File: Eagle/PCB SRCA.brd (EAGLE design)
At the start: 160 x 100 mm, 75 parts, among them IC1 DSPIC30F4011-30I_P, IC2 LM324LVIDR, IC3 LMT86QDCKRQ1, IC5 FT232RL-REEL, J1 TBL002A-350-03GR-2OR, J2 TBL002A-350-03GR-2OR, J3 TBL002A-350-03GR-2OR, J4 44914-0801, J6 TBL002A-350-03GR-2OR, J7 44914-0401, Q1 TIP41C, T1 2N3904, T12 2N3904, T13 2N3904, T2 2N3904, T3 2N3904, T4 2N3904, T5 2N3904, T6 2N3904, T7 2N3904

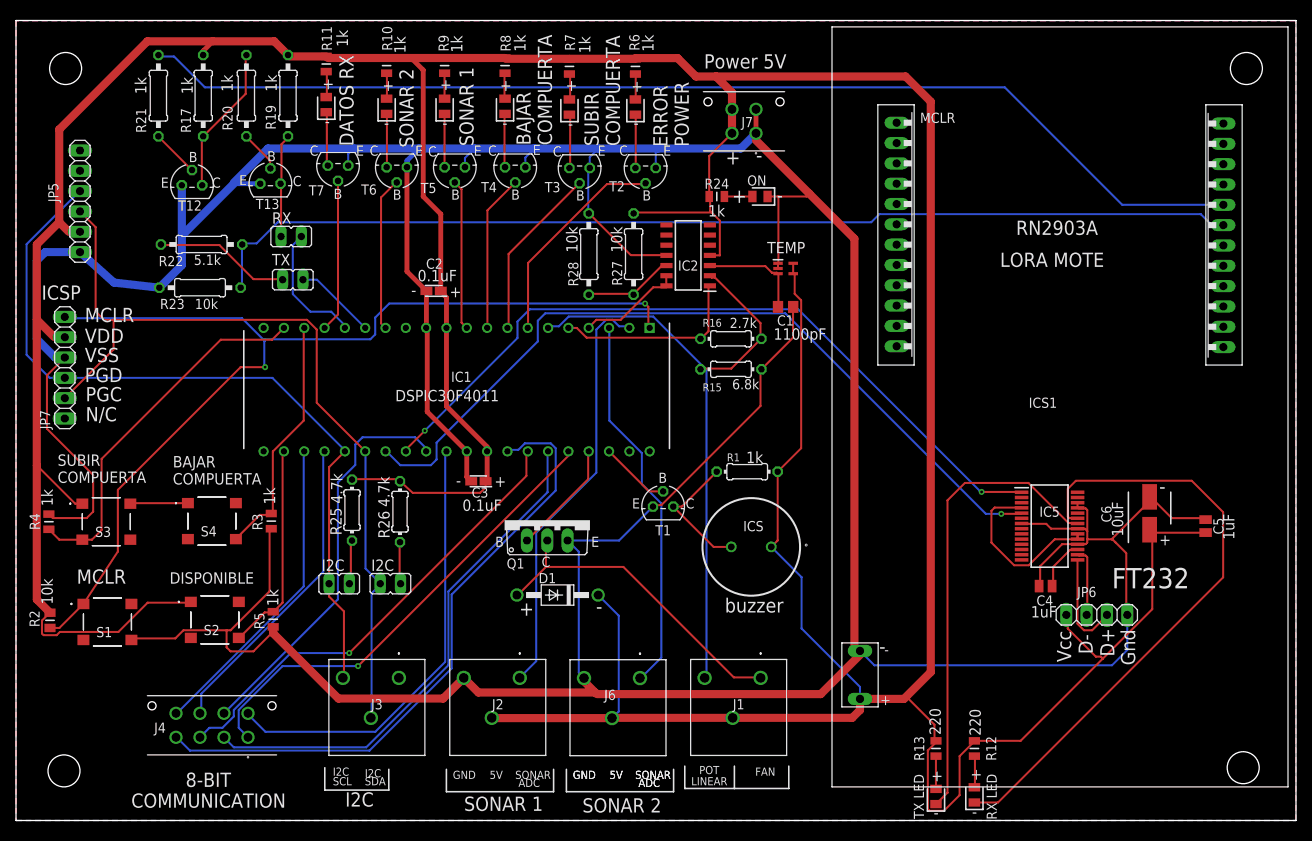
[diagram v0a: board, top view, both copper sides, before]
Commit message: 24-08-2021
correccion de errores en pistas
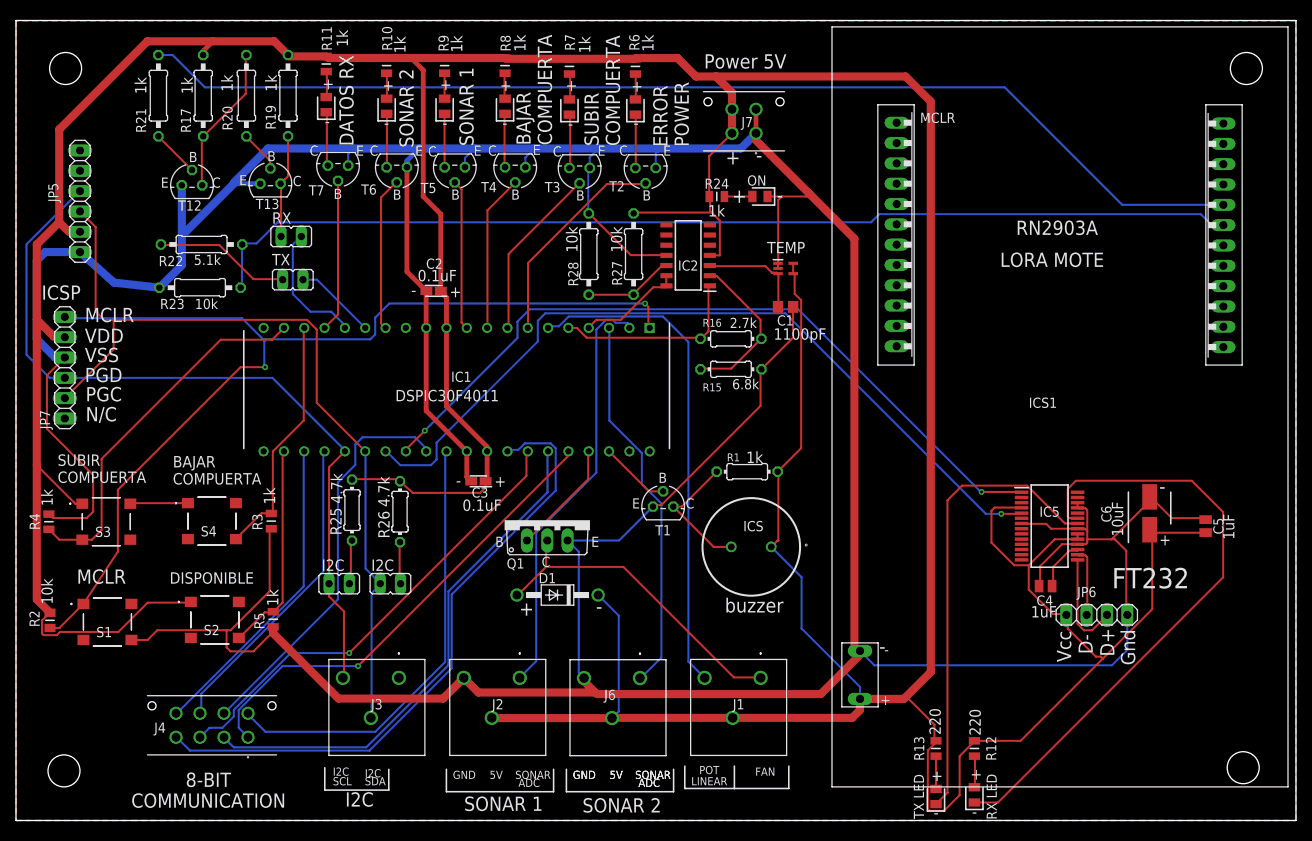
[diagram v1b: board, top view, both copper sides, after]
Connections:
- removed net N$14: IC5.19, IC5.20, IC5.4
- net V+: now also IC5.19, IC5.20, IC5.4
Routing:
- net V+: track 622.5 -> 652.4 mm
- net N$14: track 22.2 -> 0.00 mm
- net GND: track 597.9 -> 596.3 mm
- net GATE_DOWN: track 46.7 -> 46.1 mm
- net POT_LINEAR: track 61.8 -> 62.3 mm

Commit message: 26-08-2021
Actulizacion de la pcb correccion de pistas separacion entre ellas
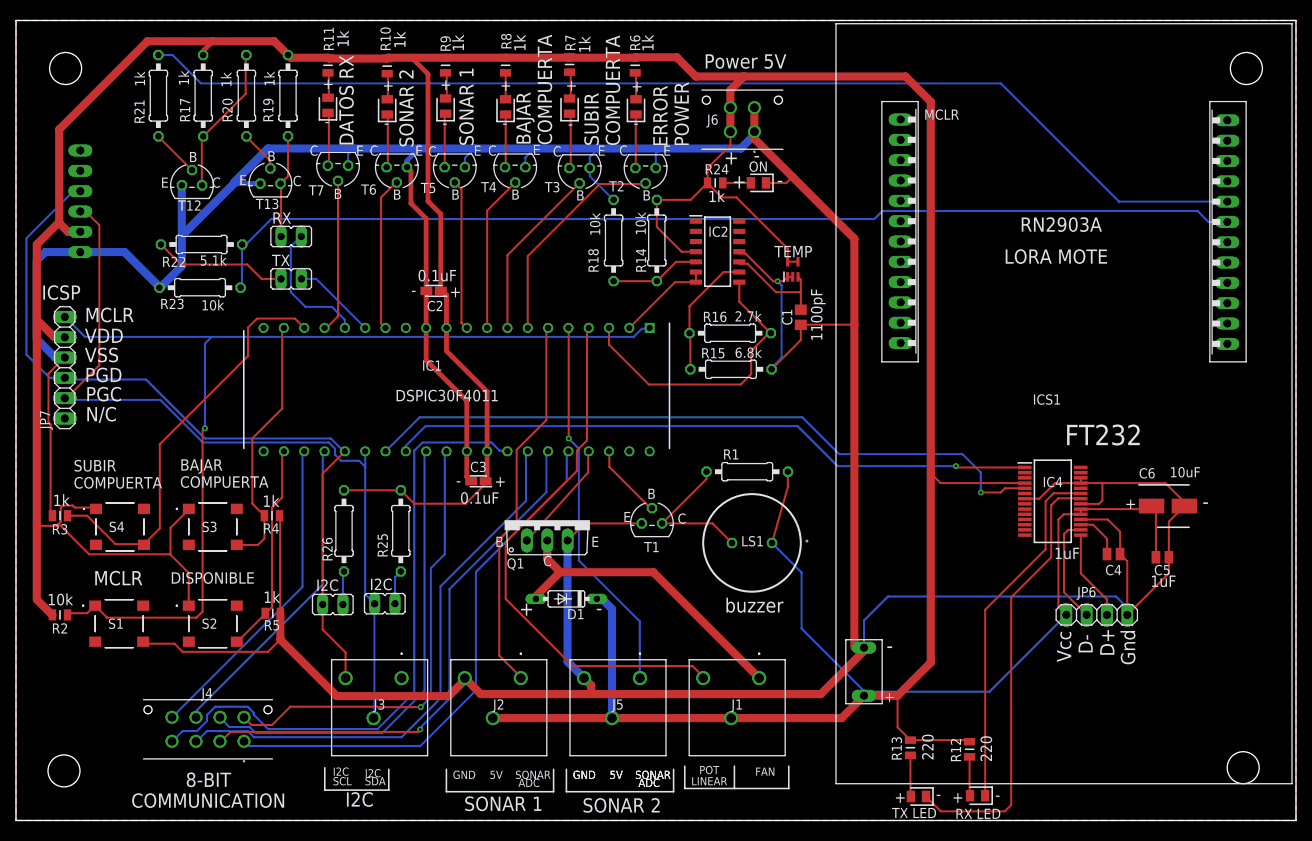
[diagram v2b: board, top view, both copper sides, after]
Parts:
- removed IC5: FT232RL-REEL, FT232RL-REEL:SOP65P778X200-28N
- removed ICS: PS1240P02BT, PS1240P02BT:PS1240P02BT
- removed J7: 44914-0401, 44914-0401:44914-0401
- removed ON: 599-0181-007F, 599-0181-007F:LEDC2012X70N
- removed R27, R28: (no value), rcl:0207/10
- added IC4: FT232RL-REEL, FT232RL-REEL:SOP65P778X200-28N
- added J5: TBL002A-350-03GR-2OR, TBL002A-350-03GR-2OR:TBL002A35003GR2OR
- added LED9: 599-0181-007F, 599-0181-007F:LEDC2012X70N
- added LS1: PS1240P02BT, PS1240P02BT:PS1240P02BT
- added R14, R18: 10k, rcl:0207/10
- D1: value 1N4004 -> 1N4148DO35-7; device diode:DO41-10 -> diode:DO35-7
- J6: value TBL002A-350-03GR-2OR -> 44914-0401; device TBL002A-350-03GR-2OR:TBL002A35003GR2OR -> 44914-0401:44914-0401
- R1: value (none) -> 1k; device rcl:0204/7 -> rcl:0207/10
- R15: value (none) -> 6.8k; device rcl:0204/7 -> rcl:0207/10
- R16: value (none) -> 2.7k; device rcl:0204/7 -> rcl:0207/10
- R17, R19, R20, R21: value (none) -> 1k
- R2: value ERA-6VEB1002V -> RC0805FR-071KL; device ERA-6VEB1002V:RESC2012X65N -> RC0805FR-071KL:RESC2012X60N
- R22: value (none) -> 5.1k
- R23: value (none) -> 10k
- R25, R26: value (none) -> 4.7k; device rcl:0204/7 -> rcl:0207/10
- moved J6 69.8 mm to (92.3, 86.1), turned to 0 degrees
- moved R4 27.9 mm to (32.0, 38.1), turned to 180 degrees
- moved R3 26.4 mm to (5.50, 38.1), turned to 0 degrees
- moved S3 13.3 mm to (24.6, 36.7)
- moved S4 11.5 mm to (13.0, 36.7)
- moved C4 9.39 mm to (137.2, 33.3), turned to 180 degrees
- moved R26 7.40 mm to (41.0, 36.2)
- moved C5 6.66 mm to (143.3, 32.9), turned to 180 degrees
- moved R25 6.63 mm to (48.1, 36.2)
- moved IC2 3.71 mm to (87.7, 71.1), turned to 0 degrees
- moved R13 3.20 mm to (111.8, 9.10)
- moved JP4 2.72 mm to (39.6, 27.0)
- moved JP3 2.60 mm to (46.1, 27.1)
- moved T1 2.52 mm to (79.5, 37.1)
- moved C6 2.47 mm to (144.0, 39.3), turned to 0 degrees
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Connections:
- removed net LMT86: C1.1, IC2.3, IC3.3
- removed net N$15 (its old number): IC5.23, LED7.1
- removed net RESISTENCIA: IC2.2, R15.2, R16.2
- removed net TEMP1: JP4.1, R25.1
- removed net TEMP2: JP3.2, R26.1
- removed net TEMP3: ICS.2, R1.1, T1.1
- new net N$19: JP3.2, R25.1
- new net N$25: LS1.2, R1.1, T1.1
- new net N$3: IC4.23, LED7.1
- new net N$31: JP4.1, R26.1
- new net N$32: IC2.5, R14.1, R18.2
- net GATE_DOWN: now also S3.D1; no longer S3.C1
- net GND: now also C5.1, IC4.18, IC4.21, IC4.25, IC4.26, IC4.7, J5.A2, J6.1, J6.3, LED9.1, R18.1; no longer C5.2, IC5.18, IC5.21, IC5.25, IC5.26, IC5.7, J6.A2, J7.1, J7.3, ON.1, R28.1
- net N$1: now also IC2.9, R15.2, R16.2; no longer S3.B1, S4.A1
- net N$18: now also IC4.22; no longer IC5.22
- net N$20: now also IC4.17; no longer IC5.17
- net N$21: now also IC4.16; no longer IC5.16
- net N$22: now also IC4.15; no longer IC5.15
- net N$27: now also C1.1, IC2.10, IC3.3; no longer IC2.12, R27.1, R28.2
- net N$28: now also LED9.2; no longer ON.2
- net POT_LINEAR: now also IC1.4; no longer IC1.6
- net POWER: now also IC1.2, IC2.6, IC2.7; no longer IC1.4, IC2.13, IC2.14
- net SONAR_ADC1: now also IC1.6; no longer IC1.2
- net SONAR_ADC2: now also IC1.5, J5.A1; no longer IC1.3, J6.A1
- net TEMP: now also IC1.3, IC2.8; no longer IC1.5, IC2.1
- net UART_RX_2: now also IC4.1; no longer IC5.1
- net UART_TX_2: now also IC4.5; no longer IC5.5
- net V+: now also C5.2, IC4.19, IC4.20, IC4.4, J5.B1, J6.2, J6.4, LS1.1, R14.2, S4.A1; no longer C5.1, IC5.19, IC5.20, IC5.4, ICS.1, J6.B1, J7.2, J7.4, R27.2
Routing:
- net N$15 (its old number): track 77.1 -> 0.00 mm
- net N$3: track 0.00 -> 44.8 mm
- net V+: track 652.4 -> 621.0 mm
- net GND: track 596.3 -> 568.4 mm, vias 0 -> 1
- net GATE_UP: track 31.2 -> 51.6 mm
- net RESISTENCIA: track 20.2 -> 0.00 mm
- net N$25: track 0.00 -> 18.5 mm
- net TEMP3: track 16.6 -> 0.00 mm
- net UART_TX_2: track 101.3 -> 87.2 mm
- net UART_RX_2: track 95.1 -> 81.2 mm, vias 2 -> 1
- net GATE_DOWN: track 46.1 -> 32.4 mm
- net LMT86: track 13.2 -> 0.00 mm
- net TEMP: track 24.3 -> 36.7 mm
- net N$32: track 0.00 -> 11.3 mm
- net BIT_3: track 58.0 -> 68.8 mm, vias 1 -> 0
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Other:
- board text added: "ON"
- board text removed: "2.7k"
- board text removed: "4.7k"
- board text removed: "5.1k"
- board text removed: "6.8k"
- board text removed: "C:/Users/ASUS/Dropbox/Trabajo de grado y PyR/imagenes/SI2C.bmp"
- board text removed: "C:/Users/ASUS/Dropbox/Trabajo de grado y PyR/imagenes/nombre.bmp"

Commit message: 31-08-2021
se agregaron las librerías del proyecto se hizo algunas correciones en la parte de el sensor de temperatura y se hizo se coloco un regulador de 5V a 3.3V para la lora mote
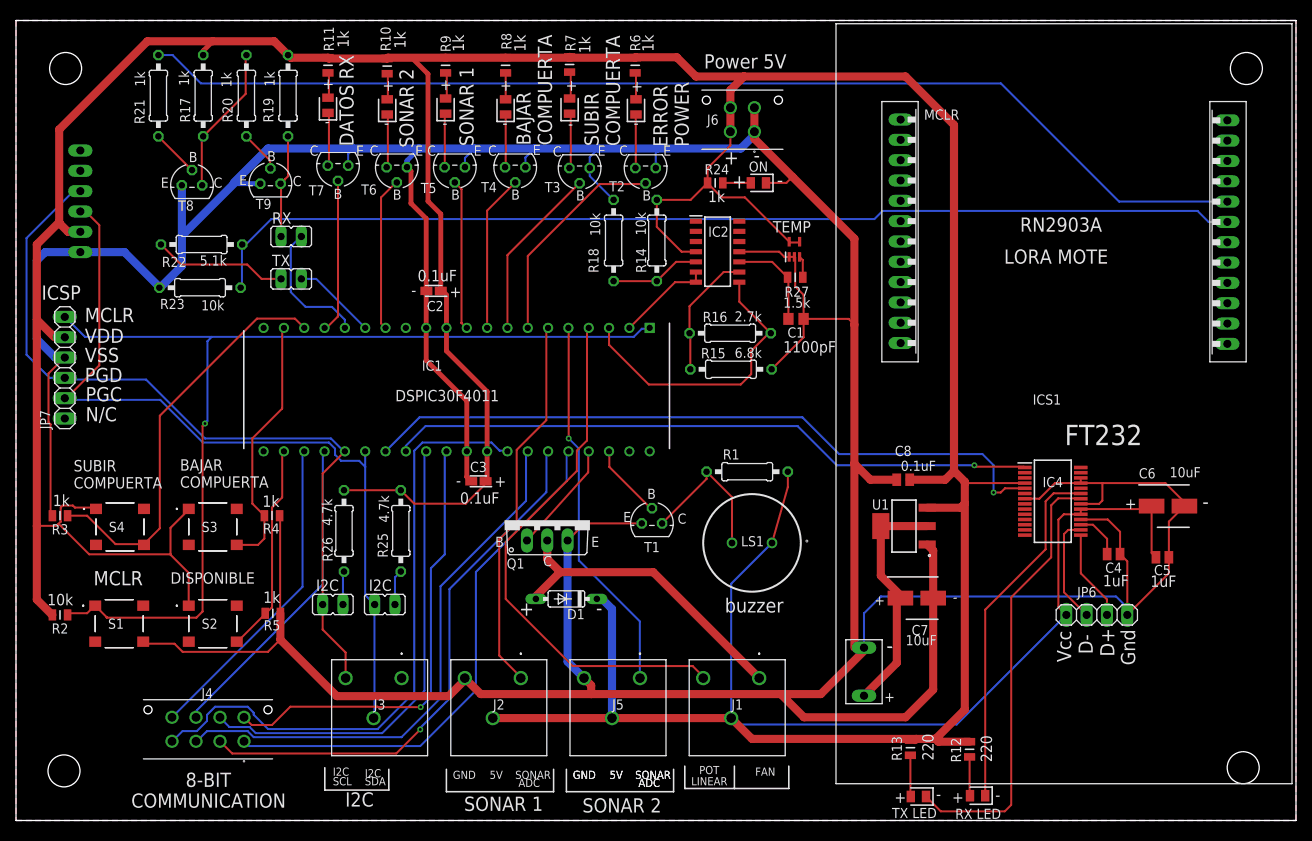
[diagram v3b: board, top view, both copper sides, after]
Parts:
- added C7: UUP1C100MCL1GS, UUP1C100MCL1GS:CAPAE530X610N
- added C8: C0805X104K1RAC3316, C0805X104K1RAC3316:CAPC2012X100N
- added R27: RC0805FR-071KL, RC0805FR-071KL:RESC2012X60N
- added U1: LD1117S33TR, LD1117S33TR:SOT230P700X180-4N
- moved IC3 2.51 mm to (97.3, 71.4)
- moved C1 0.63 mm to (97.5, 62.7), turned to 0 degrees
- moved JP3 0.10 mm to (46.1, 27.0)
- renumbered T12 to T8, T13 to T9
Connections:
- new net 3.3V: C7.1, ICS1.V5, U1.2, U1.4
- new net N$14: IC3.3, R27.2
- net GND: now also C7.2, C8.2, U1.1
- net N$27: now also R27.1; no longer IC3.3
- net V+: now also C8.1, U1.3; no longer ICS1.V5
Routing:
- net GND: track 568.4 -> 611.1 mm, vias 1 -> 0
- net 3.3V: track 0.00 -> 29.9 mm
- net V+: track 621.0 -> 647.0 mm
- net N$14: track 0.00 -> 2.72 mm
- net N$27: track 13.6 -> 12.1 mm
- net BIT_2: track 67.0 -> 68.3 mm
- net UART_TX_2: track 87.2 -> 87.8 mm
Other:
- board text added: "1.5k"

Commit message: 04-09-2021
cambios de la nueva pcb se agrego cambios del uart entre dspic y lora
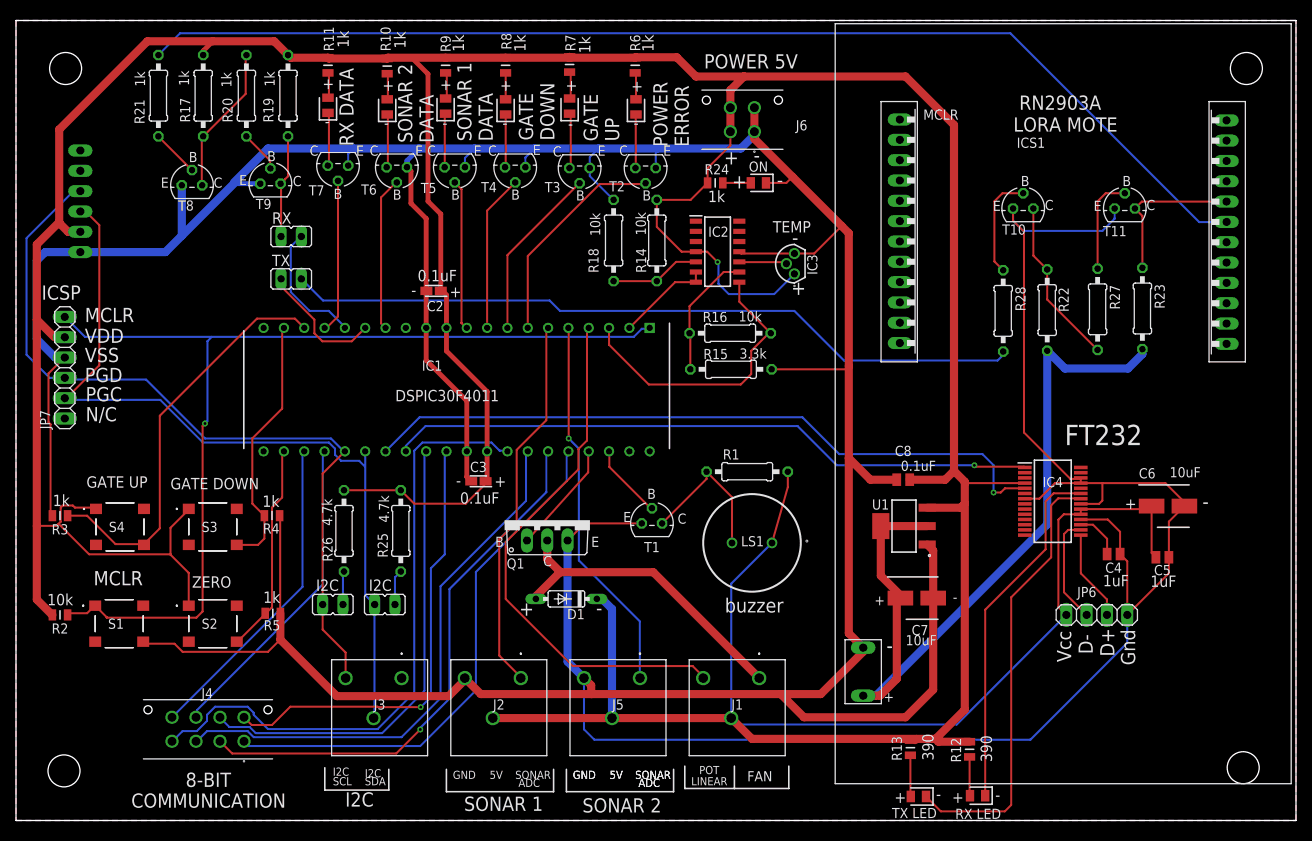
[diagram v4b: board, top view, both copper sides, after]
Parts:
- removed C1: (no value), rcl:C0805
- added R28: 1k, rcl:0207/10
- added T10, T11: 2N3904, transistor-neu-to92:TO92
- IC3: value LMT86QDCKRQ1 -> LM35DZ_NOPB; device LMT86QDCKRQ1:SOT65P210X110-5N -> LM35DZ_NOPB:LP0003A
- R15: value 6.8k -> 3.3k
- R16: value 2.7k -> 10k
- R22: value 5.1k -> 1k
- R23: value 10k -> 1k
- R27: value RC0805FR-071KL -> 1k; device RC0805FR-071KL:RESC2012X60N -> rcl:0207/10
- moved R23 117.8 mm to (140.8, 64.0), turned to 270 degrees
- moved R22 106.0 mm to (128.9, 63.8), turned to 270 degrees
- moved R27 38.0 mm to (135.2, 63.9), turned to 270 degrees
- moved IC3 2.06 mm to (96.3, 69.6)
- moved ICS1 0.10 mm to (131.4, 58.6)
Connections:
- new net N$33: R28.1, T10.2
- new net N$34: R27.1, T11.2
- net 3.3V: now also R22.2, R23.2
- net GND: now also IC3.3, T10.3, T11.3; no longer C1.2, IC3.1, IC3.2, R23.1
- net N$14: now also IC2.10, IC3.2; no longer IC3.3, R27.2
- net N$27: now also R22.1, R27.2, T10.1; no longer C1.1, IC2.10, R27.1
- net N$29: now also JP2.2, R28.2; no longer JP2.1, R22.2
- net RX_LORA: now also ICS1.UARTRX, R23.1, T11.1; no longer ICS1.UARTTX, R22.1, R23.2
- net TX_LORA: now also ICS1.UARTTX; no longer ICS1.UARTRX
- net TX_UART: now also JP2.1; no longer JP2.2
- net V+: now also IC3.1; no longer IC3.4, IC3.5
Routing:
- net RX_LORA: track 131.0 -> 19.6 mm
- net GND: track 611.1 -> 698.0 mm
- net N$29: track 16.8 -> 92.7 mm
- net 3.3V: track 29.9 -> 98.9 mm
- net N$33: track 0.00 -> 13.1 mm
- net N$34: track 0.00 -> 12.2 mm
- net N$27: track 12.1 -> 21.0 mm
- net TX_UART: track 10.5 -> 16.0 mm
- net N$14: track 2.72 -> 6.01 mm
- net TX_LORA: track 141.2 -> 144.4 mm
- net V+: track 647.0 -> 649.5 mm, vias 0 -> 1
- net RX_UART: track 16.7 -> 16.2 mm
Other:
- board text added: "390"
- board text added: "GATE DOWN"
- board text added: "GATE UP"
- board text added: "POWER 5V"
- board text added: "POWER ERROR"
- board text added: "RX DATA"
- board text added: "SONAR 1 DATA"
- board text added: "SONAR 2 DATA"
- board text added: "ZERO"
- board text removed: "1.5k"
- board text removed: "1100pF"
- board text removed: "220"
- board text removed: "BAJAR COMPUERTA"
- board text removed: "DATOS RX"
- board text removed: "DISPONIBLE"
- board text removed: "ERROR POWER"
- board text removed: "Power 5V"
- board text removed: "SUBIR COMPUERTA"
